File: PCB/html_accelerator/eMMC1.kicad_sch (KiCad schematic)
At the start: 16 parts, among them U2 AU6438BS, U5 EMMC_4G, U6 EMMC_4G, U7 EMMC_4G, Y1 12MHz

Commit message: 3d part models, PCB netlist imported
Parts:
- C2, C27: footprint (none) -> Capacitor_SMD:C_0805_2012Metric_Pad1.18x1.45mm_HandSolder
- R20: footprint (none) -> Resistor_SMD:R_0805_2012Metric_Pad1.20x1.40mm_HandSolder
- U5, U6, U7: footprint EMMC04G-M627-X03U_KNT -> html_accel_footprints:EMMC04G-M627-X03U_KNT
- Y1: footprint (none) -> Crystal:Crystal_SMD_HC49-SD
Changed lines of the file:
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@@
       (effects (font (size 1.27 1.27)))
     )
-    (property "Footprint" "" (at 116.586 48.514 90)
+    (property "Footprint" "Resistor_SMD:R_0805_2012Metric_Pad1.20x1.40mm_HandSolder" (at 116.586 48.514 90)
       (effects (font (size 1.27 1.27)) hide)
     )
@@
       (effects (font (size 1.524 1.524)))
     )
-    (property "Footprint" "EMMC04G-M627-X03U_KNT" (at 171.45 48.26 0)
+    (property "Footprint" "html_accel_footprints:EMMC04G-M627-X03U_KNT" (at 171.45 48.26 0)
       (effects (font (size 1.27 1.27) italic) hide)
     )
@@
       (effects (font (size 1.524 1.524)))
     )
-    (property "Footprint" "EMMC04G-M627-X03U_KNT" (at 231.14 48.26 0)
+    (property "Footprint" "html_accel_footprints:EMMC04G-M627-X03U_KNT" (at 231.14 48.26 0)
       (effects (font (size 1.27 1.27) italic) hide)
     )
@@
       (effects (font (size 1.27 1.27)))
     )
-    (property "Footprint" "" (at 56.896 101.854 90)
+    (property "Footprint" "Resistor_SMD:R_0805_2012Metric_Pad1.20x1.40mm_HandSolder" (at 56.896 101.854 90)
       (effects (font (size 1.27 1.27)) hide)
     )
@@
       (effects (font (size 1.27 1.27)))
     )
-    (property "Footprint" "" (at 48.5648 106.68 0)
+    (property "Footprint" "Capacitor_SMD:C_0805_2012Metric_Pad1.18x1.45mm_HandSolder" (at 48.5648 106.68 0)
       (effects (font (size 1.27 1.27)) hide)
     )
@@
       (effects (font (size 1.27 1.27)))
     )
-    (property "Footprint" "" (at 33.3248 106.68 0)
+    (property "Footprint" "Capacitor_SMD:C_0805_2012Metric_Pad1.18x1.45mm_HandSolder" (at 33.3248 106.68 0)
       (effects (font (size 1.27 1.27)) hide)
     )
@@
       (effects (font (size 1.27 1.27)) (justify left))
     )
-    (property "Footprint" "" (at 123.4948 120.65 0)
+    (property "Footprint" "Capacitor_SMD:C_0805_2012Metric_Pad1.18x1.45mm_HandSolder" (at 123.4948 120.65 0)
       (effects (font (size 1.27 1.27)) hide)
     )
@@
       (effects (font (size 1.27 1.27)) (justify left))
     )
-    (property "Footprint" "" (at 134.9248 120.65 0)
+    (property "Footprint" "Capacitor_SMD:C_0805_2012Metric_Pad1.18x1.45mm_HandSolder" (at 134.9248 120.65 0)
       (effects (font (size 1.27 1.27)) hide)
     )
@@
       (effects (font (size 1.27 1.27)) (justify left))
     )
-    (property "Footprint" "" (at 136.8552 97.79 0)
+    (property "Footprint" "Capacitor_SMD:C_0805_2012Metric_Pad1.18x1.45mm_HandSolder" (at 136.8552 97.79 0)
       (effects (font (size 1.27 1.27)) hide)
     )
@@
       (effects (font (size 1.27 1.27)))
     )
-    (property "Footprint" "" (at 52.324 77.724 90)
+    (property "Footprint" "Resistor_SMD:R_0805_2012Metric_Pad1.20x1.40mm_HandSolder" (at 52.324 77.724 90)
       (effects (font (size 1.27 1.27)) hide)
     )
@@
       (effects (font (size 1.27 1.27)))
     )
-    (property "Footprint" "" (at 137.414 80.264 90)
+    (property "Footprint" "Resistor_SMD:R_0805_2012Metric_Pad1.20x1.40mm_HandSolder" (at 137.414 80.264 90)
       (effects (font (size 1.27 1.27)) hide)
     )
@@
       (effects (font (size 1.27 1.27)) (justify left))
     )
-    (property "Footprint" "" (at 125.4252 97.79 0)
+    (property "Footprint" "Capacitor_SMD:C_0805_2012Metric_Pad1.18x1.45mm_HandSolder" (at 125.4252 97.79 0)
       (effects (font (size 1.27 1.27)) hide)
     )
@@
       (effects (font (size 1.27 1.27)) (justify left))
     )
-    (property "Footprint" "" (at 147.0152 127 0)
+    (property "Footprint" "Capacitor_SMD:C_0805_2012Metric_Pad1.18x1.45mm_HandSolder" (at 147.0152 127 0)
       (effects (font (size 1.27 1.27)) hide)
     )
@@
       (effects (font (size 1.27 1.27)))
     )
-    (property "Footprint" "" (at 41.91 95.25 0)
-      (effects (font (size 1.27 1.27)) hide)
-    )
-    (property "Datasheet" "~" (at 41.91 95.25 0)
+    (property "Footprint" "Crystal:Crystal_SMD_HC49-SD" (at 41.91 95.25 0)
+      (effects (font (size 1.27 1.27)) hide)
+    )
+    (property "Datasheet" "12M20P2/49SMT" (at 41.91 95.25 0)
       (effects (font (size 1.27 1.27)) hide)
     )
@@
       (effects (font (size 1.524 1.524)))
     )
-    (property "Footprint" "EMMC04G-M627-X03U_KNT" (at 269.24 48.26 0)
+    (property "Footprint" "html_accel_footprints:EMMC04G-M627-X03U_KNT" (at 269.24 48.26 0)
       (effects (font (size 1.27 1.27) italic) hide)
     )

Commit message: placement updates
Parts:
- Y1: footprint Crystal:Crystal_SMD_HC49-SD -> Crystal:Crystal_SMD_3225-4Pin_3.2x2.5mm
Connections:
- net +3V3 renamed +5V
- no-connect marks 125 -> 2

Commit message: layout and 3d updates
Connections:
- net DATA_0: now reaches U2.27 (DATA0), U5.A3 (DAT0)
- net DATA_1: now reaches U2.28 (DATA1), U5.A4 (DAT1)
- net DATA_2: now reaches U2.19 (DATA2), U5.A5 (DAT2)
- net DATA_3: now reaches U2.20 (DATA3), U5.B2 (DAT3)
- net DATA_4: now reaches U2.21 (DATA4), U5.B3 (DAT4)
- net DATA_5: now reaches U2.23 (DATA5), U5.B4 (DAT5)
- net DATA_6: now reaches U2.25 (DATA6), U5.B5 (DAT6)
- net DATA_7: now reaches U2.26 (DATA7), U5.B6 (DAT7)
- net USB0_DM renamed 90_USB0_D_P
- net USB0_DP renamed 90_USB0_D_N
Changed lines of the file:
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@@
+    (effects (font (size 1.27 1.27)) (justify left bottom))
+  )
+  (label "DATA_7" (at 115.57 76.2 0) (fields_autoplaced)
+    (effects (font (size 1.27 1.27)) (justify left bottom))
+  )
+  (label "DATA_1" (at 115.57 60.96 0) (fields_autoplaced)
+    (effects (font (size 1.27 1.27)) (justify left bottom))
+  )
+  (label "DATA_2" (at 115.57 63.5 0) (fields_autoplaced)
+    (effects (font (size 1.27 1.27)) (justify left bottom))
+  )
+  (label "DATA_3" (at 115.57 66.04 0) (fields_autoplaced)
+    (effects (font (size 1.27 1.27)) (justify left bottom))
+  )
+  (label "DATA_6" (at 115.57 73.66 0) (fields_autoplaced)
+    (effects (font (size 1.27 1.27)) (justify left bottom))
+  )
+  (label "DATA_5" (at 115.57 71.12 0) (fields_autoplaced)
+    (effects (font (size 1.27 1.27)) (justify left bottom))
+  )
+  (label "DATA_4" (at 115.57 68.58 0) (fields_autoplaced)
+    (effects (font (size 1.27 1.27)) (justify left bottom))
+  )
+  (label "DATA_0" (at 115.57 58.42 0) (fields_autoplaced)
     (effects (font (size 1.27 1.27)) (justify left bottom))
   )
@@
     )
   )
-  (global_label "USB0_DP" (shape bidirectional) (at 34.29 71.12 180) (fields_autoplaced)
+  (global_label "90_USB0_D_N" (shape bidirectional) (at 34.29 71.12 180) (fields_autoplaced)
     (effects (font (size 1.27 1.27)) (justify right))
-    (property "Intersheetrefs" "${INTERSHEET_REFS}" (at 21.7458 71.12 0)
+    (property "Intersheetrefs" "${INTERSHEET_REFS}" (at 17.3311 71.12 0)
       (effects (font (size 1.27 1.27)) (justify right))
     )
   )
-  (global_label "USB0_DM" (shape bidirectional) (at 34.29 66.04 180) (fields_autoplaced)
+  (global_label "90_USB0_D_P" (shape bidirectional) (at 34.29 66.04 180) (fields_autoplaced)
     (effects (font (size 1.27 1.27)) (justify right))
-    (property "Intersheetrefs" "${INTERSHEET_REFS}" (at 21.5644 66.04 0)
+    (property "Intersheetrefs" "${INTERSHEET_REFS}" (at 17.3916 66.04 0)
       (effects (font (size 1.27 1.27)) (justify right))
     )

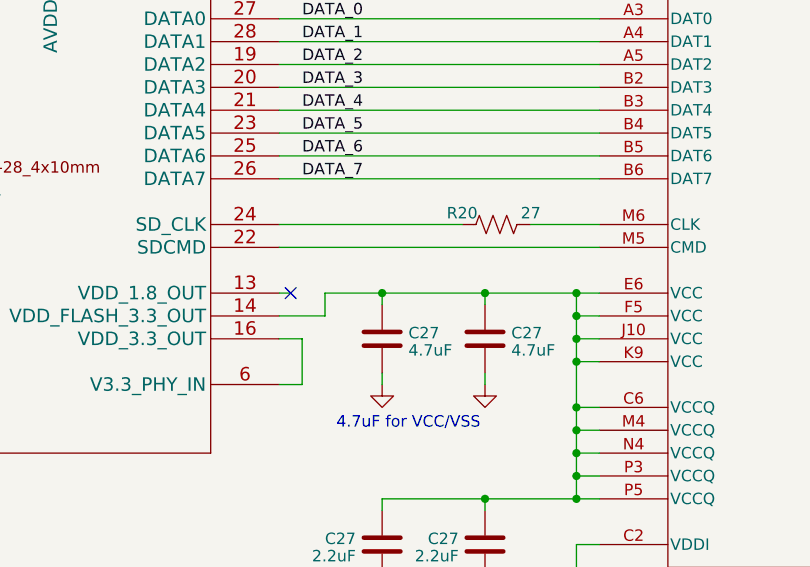
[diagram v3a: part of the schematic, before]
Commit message: impedance controlled nets
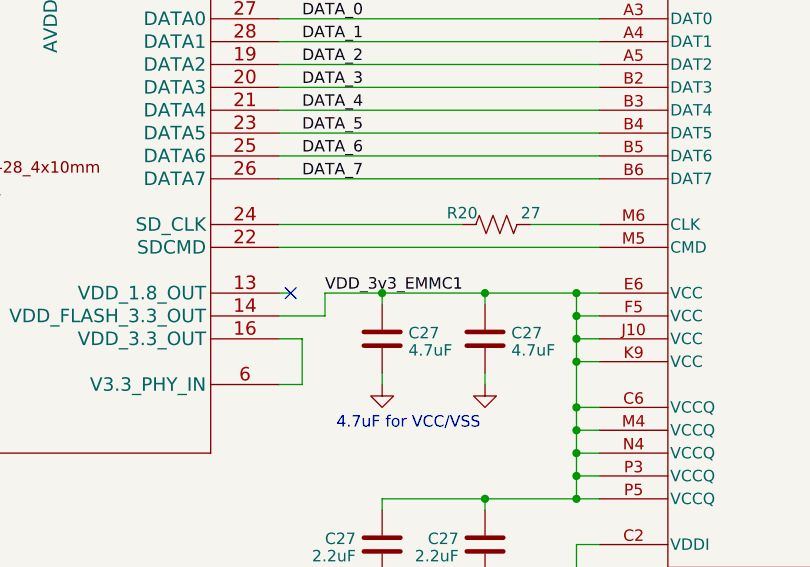
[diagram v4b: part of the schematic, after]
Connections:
- net VDD_3v3_EMMC1: now reaches C27.1, C27.1, C27.1, C27.1, U2.14 (VDD_FLASH_3.3_OUT), U5.C6 (VCCQ), U5.E6 (VCC), U5.F5 (VCC), U5.J10 (VCC), U5.K9 (VCC), U5.M4 (VCCQ), U5.N4 (VCCQ), U5.P3 (VCCQ), U5.P5 (VCCQ)
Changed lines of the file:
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@@
+    (effects (font (size 1.27 1.27)) (justify left bottom))
+  )
+  (label "VDD_3v3_EMMC1" (at 118.11 88.9 0) (fields_autoplaced)
     (effects (font (size 1.27 1.27)) (justify left bottom))
   )

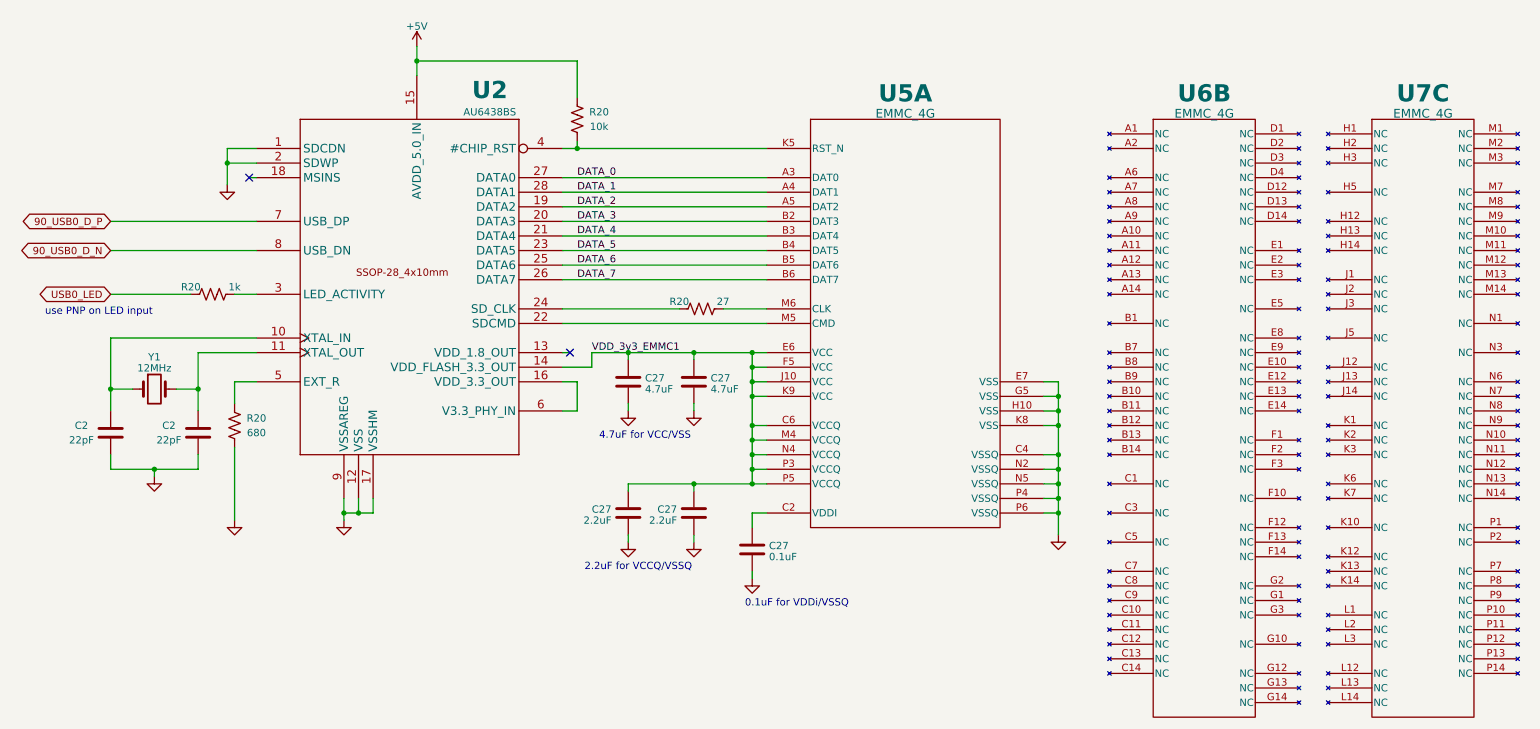
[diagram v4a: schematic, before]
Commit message: constraints for impedance control
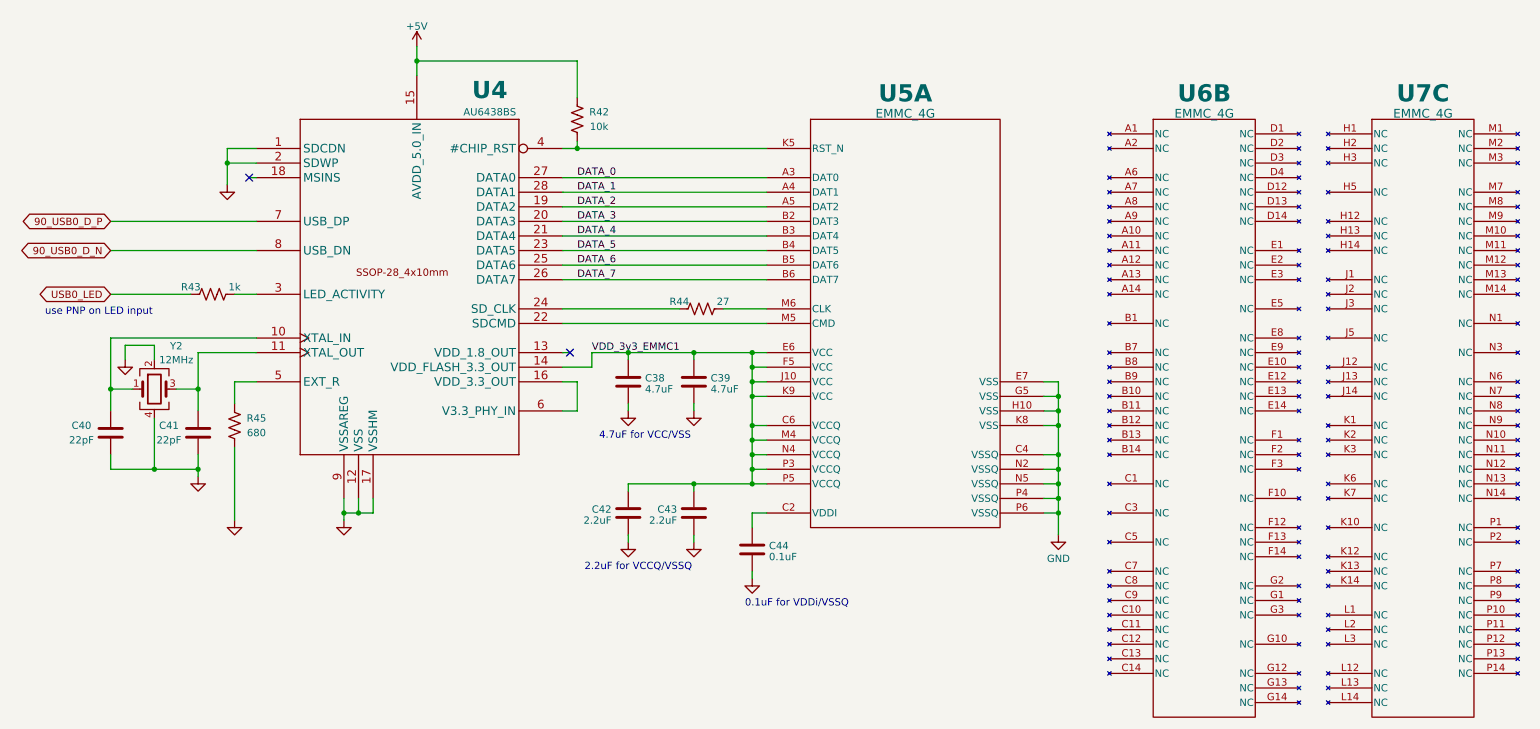
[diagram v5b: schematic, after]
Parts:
- removed Y1: 12MHz, Crystal:Crystal_SMD_3225-4Pin_3.2x2.5mm, symbol Device:Crystal
- added Y2: 12MHz, Crystal:Crystal_SMD_3225-4Pin_3.2x2.5mm, symbol Device:Crystal_GND24
- renumbered C27 to C38, C27 to C39, C2 to C40, C2 to C41, C27 to C42, C27 to C43, C27 to C44, R20 to R42, R20 to R43, R20 to R44, R20 to R45, U2 to U4
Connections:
- net GND: now also Y2.2, Y2.4
- net at C41.1, U4.11 (XTAL_OUT): now also Y2.3
- net at C40.1, U4.10 (XTAL_IN): now also Y2.1

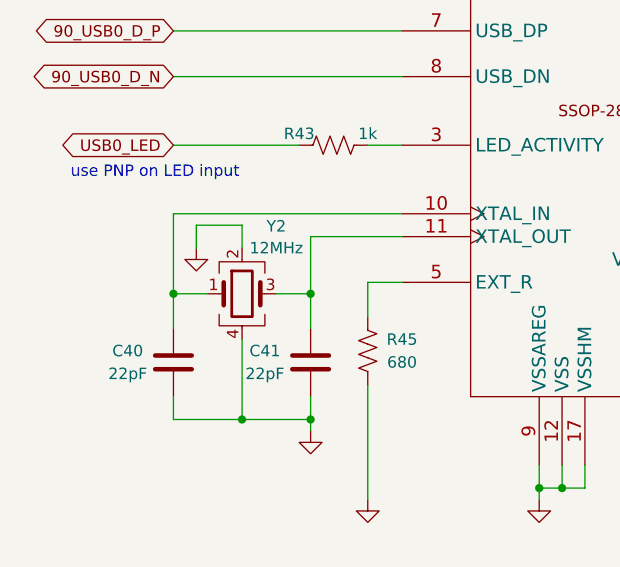
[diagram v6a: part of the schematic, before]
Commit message: Additional routing greebles, cleanup and gerber export with BOM
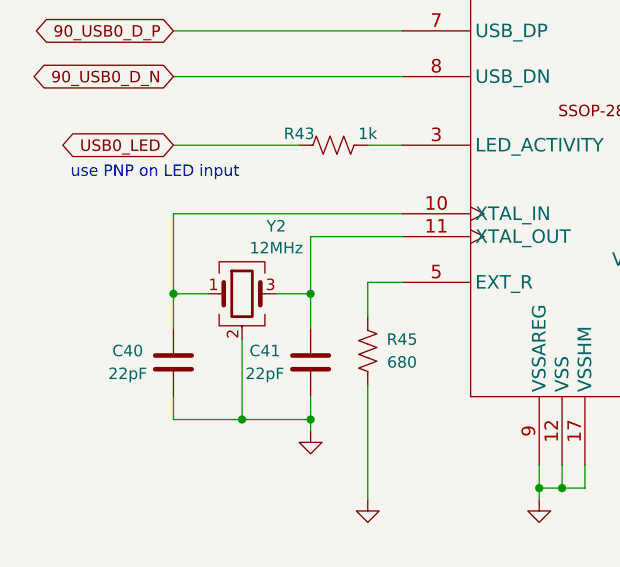
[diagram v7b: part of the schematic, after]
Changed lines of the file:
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@@
 	(wire
 		(pts
-			(xy 41.91 90.17) (xy 41.91 87.63)
-		)
-		(stroke
-			(width 0)
-			(type default)
-		)
-	)
-	(wire
-		(pts
 			(xy 59.69 93.98) (xy 55.88 93.98)
 		)
@@
 	(wire
 		(pts
-			(xy 41.91 87.63) (xy 36.83 87.63)
-		)
-		(stroke
-			(width 0)
-			(type default)
-		)
-	)
-	(wire
-		(pts
 			(xy 74.93 114.3) (xy 74.93 116.84)
 		)
@@
 	(wire
 		(pts
-			(xy 36.83 87.63) (xy 36.83 90.17)
-		)
-		(stroke
-			(width 0)
-			(type default)
-		)
-	)
-	(wire
-		(pts
 			(xy 196.85 101.6) (xy 199.39 101.6)
 		)
@@
 	)
 	(symbol
-		(lib_id "power:GND")
-		(at 36.83 90.17 0)
-		(unit 1)
-		(body_style 1)
-		(exclude_from_sim no)
-		(in_bom yes)
-		(on_board yes)
-		(in_pos_files yes)
-		(dnp no)
-		(fields_autoplaced yes)
-		(property "Reference" "#PWR050"
-			(at 36.83 96.52 0)
-			(hide yes)
-			(show_name no)
-			(do_not_autoplace no)
-			(effects
-				(font
-					(size 1.27 1.27)
-				)
-			)
-		)
-		(property "Value" "GND"
-			(at 36.83 94.3055 0)
-			(hide yes)
-			(show_name no)
-			(do_not_autoplace no)
-			(effects
-				(font
-					(size 1.27 1.27)
-				)
-			)
-		)
-		(property "Footprint" ""
-			(at 36.83 90.17 0)
-			(hide yes)
-			(show_name no)
-			(do_not_autoplace no)
-			(effects
-				(font
-					(size 1.27 1.27)
-				)
-			)
-		)
-		(property "Datasheet" ""
-			(at 36.83 90.17 0)
-			(hide yes)
-			(show_name no)
-			(do_not_autoplace no)
-			(effects
-				(font
-					(size 1.27 1.27)
-				)
-			)
-		)
-		(property "Description" ""
-			(at 36.83 90.17 0)
-			(show_name no)
-			(do_not_autoplace no)
-			(effects
-				(font
-					(size 1.27 1.27)
-				)
-			)
-		)
-		(pin "1"
-		)
-		(instances
-			(project "html_accelerator"
-				(path "/12b3a7c9-141f-40ba-9ebb-094b58bfa6c7/c1e0624f-11bc-46dd-864f-01b3a932cae6"
-					(reference "#PWR050")
-					(unit 1)
-				)
-			)
-		)
-	)
-	(symbol
 		(lib_id "Device:R_US")
 		(at 137.16 81.28 90)
@@
 			)
 		)
-		(property "Description" ""
+		(property "Description" "Four pin crystal, GND on pins 2 and 4"
 			(at 41.91 95.25 0)
+			(hide yes)
 			(show_name no)
 			(do_not_autoplace no)

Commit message: gerbers and readme updates
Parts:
- U5, U6, U7: value EMMC_4G -> H26M31003
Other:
- company: (none) -> Spencer K
- title: (none) -> HTML Accelerator
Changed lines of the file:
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@@
 	(generator_version "10.0")
 	(paper "A4")
+	(title_block
+		(title "HTML Accelerator")
+		(date "2026-04-25")
+		(rev "1.0")
+		(company "Spencer K")
+		(comment 1 "https://github.com/akaStanley/HTML_Accelerator")
+	)
 	(text "4.7uF for VCC/VSS"
 		(exclude_from_sim no)
@@
 			)
 		)
-		(property "Value" "EMMC_4G"
+		(property "Value" "H26M31003"
 			(at 172.72 47.2581 0)
 			(show_name no)
@@
 			)
 		)
-		(property "Value" "EMMC_4G"
+		(property "Value" "H26M31003"
 			(at 224.79 47.2581 0)
 			(show_name no)
@@
 			)
 		)
-		(property "Value" "EMMC_4G"
+		(property "Value" "H26M31003"
 			(at 262.89 47.2581 0)
 			(show_name no)
